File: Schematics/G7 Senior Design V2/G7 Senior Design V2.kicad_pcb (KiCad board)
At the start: 2 copper layers, 65 x 58.5 mm, 26 parts, among them IC1 TPS62122DRVR, IC3 CP2102N-A02-GQFN28, J1 87583-2010RLF, J2 PJ-051AH, Q1 SS8050-G, Q2 SS8050-G, U1 ESP32-WROOM-32-N4, U2 DWM1000

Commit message: Added Changes from Last Meeting
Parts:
- added C14-0.1uF1: CC0805KRX7R9BB104, SD V2 ESP32 Components:CC0805N_YAG, F.Cu at (167.4, 103.3)
- added C14-0.1uF3: CC0805KRX7R9BB104, SD V2 ESP32 Components:CC0805N_YAG, F.Cu at (188.8, 73.5)
- added C15-0.1uF4: CC0805KRX7R9BB104, SD V2 ESP32 Components:CC0805N_YAG, F.Cu at (167.4, 106.2)
- added C3-0.1uF4: CC0805KRX7R9BB104, SD V2 ESP32 Components:CC0805N_YAG, F.Cu at (167.4, 109.1)
- added C3-22uF2: LMK212BJ226MG-T, SD V2 ESP32 Components:CAP_LMK212AB7106MG-T_TAY, F.Cu at (168.1, 112.0)
- added C9-0.1uF2: CC0805KRX7R9BB104, SD V2 ESP32 Components:CC0805N_YAG, F.Cu at (188.8, 70.6)
- added LED1: HSMW-C170-U0000, SD V2 DW1000 Components:LEDC2012X90N, F.Cu at (184.2, 70.9)
- added LED2: HSMW-C170-U0000, SD V2 DW1000 Components:LEDC2012X90N, F.Cu at (184.2, 74.2)
- added LED3: HSMW-C170-U0000, SD V2 DW1000 Components:LEDC2012X90N, F.Cu at (184.2, 77.6)
- added LED4: HSMW-C170-U0000, SD V2 DW1000 Components:LEDC2012X90N, F.Cu at (184.2, 80.9)
- added LED5: HSMW-C170-U0000, SD V2 DW1000 Components:LEDC2012X90N, F.Cu at (190.4, 83.4)
- added R11-10K2: ERJ-6GEYJ103V, SD V2 USB to UART Components:RC0805N_PAN, F.Cu at (188.8, 76.4)
- added R3-0-Ohms1: RMCF0805ZT0R00, SD V2 USB to UART Components:STA_RMCF0805_STP, F.Cu at (189.1, 64.5)
- added R3-10K5: ERJ-6GEYJ103V, SD V2 USB to UART Components:RC0805N_PAN, F.Cu at (188.8, 79.2)
- added R3-10K6: ERJ-6GEYJ103V, SD V2 USB to UART Components:RC0805N_PAN, F.Cu at (190.1, 86.5)
- added R3-1K2: RG2012P-105-B-T5, SD V2 USB to UART Components:RES_1220_SUS, F.Cu at (193.1, 76.5)
- added R3-1K3: RG2012P-105-B-T5, SD V2 USB to UART Components:RES_1220_SUS, F.Cu at (186.6, 90.8)
- added R3-1K4: RG2012P-105-B-T5, SD V2 USB to UART Components:RES_1220_SUS, F.Cu at (186.6, 93.9)
- added R3-1K5: RG2012P-105-B-T5, SD V2 USB to UART Components:RES_1220_SUS, F.Cu at (190.4, 104.5)
- added S1: PTS_647_SN50_SMTR2_LFS, SD V2 ESP32 Components:SW_PTS_647_SN50_SMTR2_LFS, F.Cu at (161.1, 104.9)
- added S2: PTS_647_SN50_SMTR2_LFS, SD V2 ESP32 Components:SW_PTS_647_SN50_SMTR2_LFS, F.Cu at (161.1, 110.9)
- renumbered C3-0.1uF1 to C19-0.1uF1, C3-4.7uF1 to C20-4.7uF1, C3-22uF1 to C21-22uF1, C3-0.1uF2 to C22-0.1uF2, R3-10K3 to R21-10K3, R3-10K4 to R22-10K4, R3-10K1 to R23-10K1, R3-1K1 to R24-1K1, R3-22.1K1 to R25-22.1K1, R3-47.5K1 to R26-47.5K1
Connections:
- net Net-(U1-IO0) renamed /IO0
- C19-0.1uF1 pad 1: Net-(IC1-VOUT) -> Net-(IC3-VDD)
- C20-4.7uF1 pad 1: Net-(IC1-VOUT) -> Net-(IC3-VDD)
- C21-22uF1 pad 1: Net-(IC1-VOUT) -> Net-(IC3-VDD)
- C22-0.1uF2 pad 1: Net-(IC1-VOUT) -> Net-(IC3-VDD)
- IC3 pad 6: Net-(IC1-VOUT) -> Net-(IC3-VDD)
- IC3 pad 7: Net-(IC1-VOUT) -> Net-(IC3-VDD)
- Q1 pad 3: Net-(U1-EN) -> /EN
- R24-1K1 pad 1: Net-(IC1-VOUT) -> Net-(IC3-VDD)
- U1 pad 12: unconnected-(U1-IO27-Pad12) -> Net-(U1-IO27)
- U1 pad 2: Net-(IC1-VOUT) -> Net-(IC3-VDD)
- U1 pad 3: Net-(U1-EN) -> /EN
- U1 pad 6: unconnected-(U1-IO34-Pad6) -> Net-(U1-IO34)
- U1 pad 8: unconnected-(U1-IO32-Pad8) -> Net-(U1-IO32)
- U1 pad 9: unconnected-(U1-IO33-Pad9) -> Net-(U1-IO33)
- U2 pad 1: unconnected-(U2-EXTON-Pad1) -> Net-(U2-EXTON)
- U2 pad 12: unconnected-(U2-GPIO3/TXLED-Pad12) -> Net-(LED5-A)
- U2 pad 13: unconnected-(U2-GPIO2/RXLED-Pad13) -> Net-(LED1-A)
- U2 pad 14: unconnected-(U2-GPIO1/SFDLED-Pad14) -> Net-(LED2-A)
- U2 pad 15: unconnected-(U2-GPIO0/RXOKLED-Pad15) -> Net-(LED3-A)
- U2 pad 2: unconnected-(U2-WAKEUP-Pad2) -> Net-(U2-WAKEUP)
- U2 pad 22: unconnected-(U2-IRQ/GPIO8-Pad22) -> Net-(U1-IO34)
- U2 pad 3: unconnected-(U2-RSTN-Pad3) -> Net-(U2-RSTN)
- U2 pad 5: Net-(IC1-VOUT) -> Net-(IC3-VDD)
- U2 pad 6: Net-(IC1-VOUT) -> Net-(IC3-VDD)
- U2 pad 7: Net-(IC1-VOUT) -> Net-(IC3-VDD)
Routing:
- net Net-(U1-IO27): track 0.00 -> 32.7 mm, vias 0 -> 1
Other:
- board size 65 x 58.5 mm -> 85 x 58.5 mm

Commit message: Weeks Revision before Jungle of Words
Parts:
- moved R3-1K2 56.4 mm to (139.5, 94.0)
- moved LED4 48.0 mm to (139.3, 98.0), turned to -90 degrees
- moved LED3 46.3 mm to (142.7, 98.0), turned to -90 degrees
- moved LED2 45.0 mm to (146.0, 98.0), turned to -90 degrees
- moved LED1 44.2 mm to (149.3, 98.0), turned to -90 degrees
- moved LED5 40.1 mm to (153.0, 98.0), turned to -90 degrees
- moved R3-0-Ohms1 31.3 mm to (168.4, 88.0)
- moved S2 31.1 mm to (132.9, 97.9)
- moved S1 29.7 mm to (133.1, 114.9), turned to 180 degrees
- moved R11-10K2 28.6 mm to (164.1, 90.9)
- moved R3-10K5 28.6 mm to (164.1, 93.7)
- moved C14-0.1uF3 28.6 mm to (164.1, 88.0)
- moved C9-0.1uF2 28.6 mm to (164.1, 85.1)
- moved L1 26.2 mm to (190.4, 83.0)
- moved Cin-4.7uF1 25.8 mm to (195.9, 81.5)
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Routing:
- net GND: track 233.6 -> 405.5 mm, vias 2 -> 20
- net Net-(IC3-VDD): track 0.00 -> 148.4 mm, vias 0 -> 10
- net Net-(U1-IO19): track 37.4 -> 146.9 mm
- net /EN: track 0.00 -> 101.4 mm, vias 0 -> 5
- net Net-(U1-IO34): track 0.00 -> 71.9 mm, vias 0 -> 4
- net /IO0: track 40.6 -> 97.9 mm, vias 2 -> 4
- net Net-(U1-IO23): track 42.5 -> 98.2 mm
- net Net-(IC1-VOUT): track 144.9 -> 90.2 mm, vias 9 -> 8
- net Net-(U1-IO32): track 0.00 -> 46.3 mm, vias 0 -> 4
- net Net-(U1-IO33): track 0.00 -> 39.7 mm, vias 0 -> 4
- net Net-(U1-EN): track 40.0 -> 3.56 mm, vias 2 -> 0
- net Net-(U2-EXTON): track 0.00 -> 32.1 mm, vias 0 -> 2
- net Net-(U1-IO27): track 32.7 -> 62.2 mm, vias 1 -> 2
- net Net-(U2-WAKEUP): track 0.00 -> 28.8 mm, vias 0 -> 2
- net Net-(U1-IO4): track 23.4 -> 45.3 mm
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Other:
- board size 85 x 58.5 mm -> 85 x 73 mm

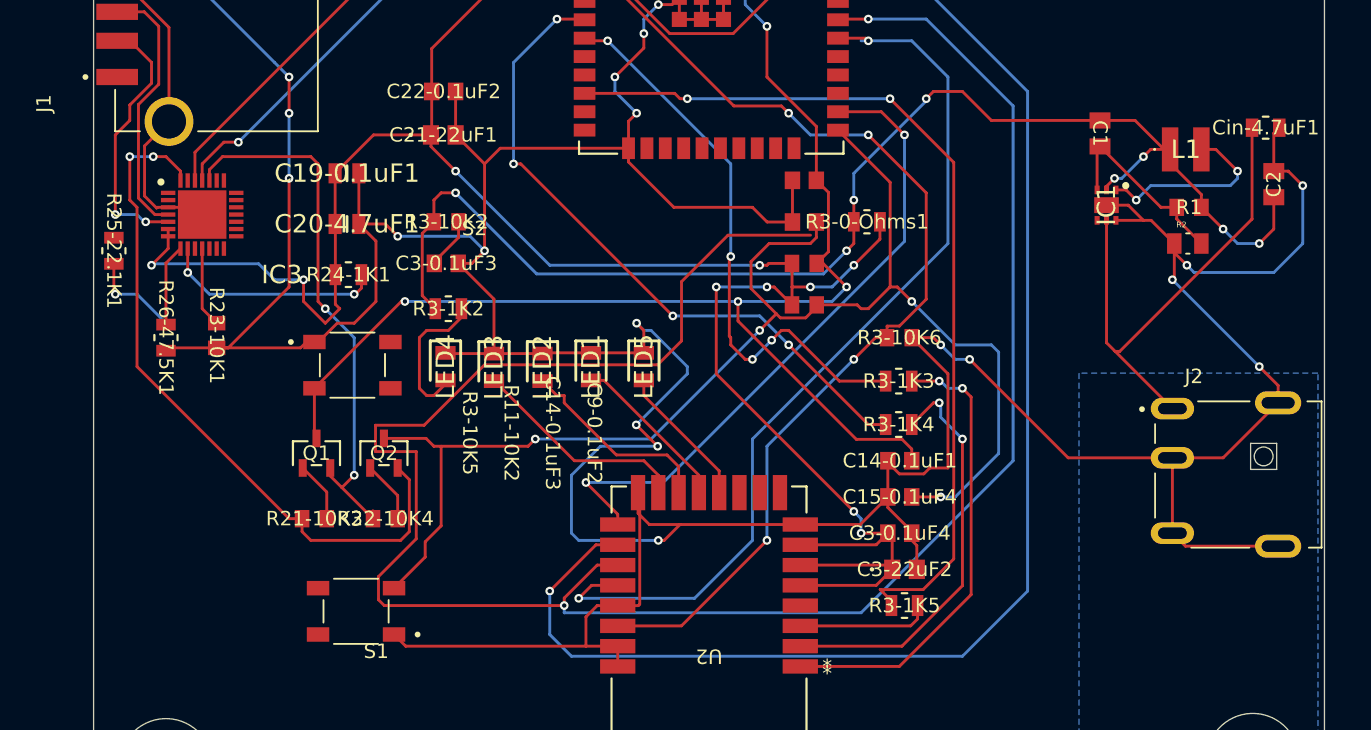
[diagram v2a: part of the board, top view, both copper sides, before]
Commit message: labels adjusted
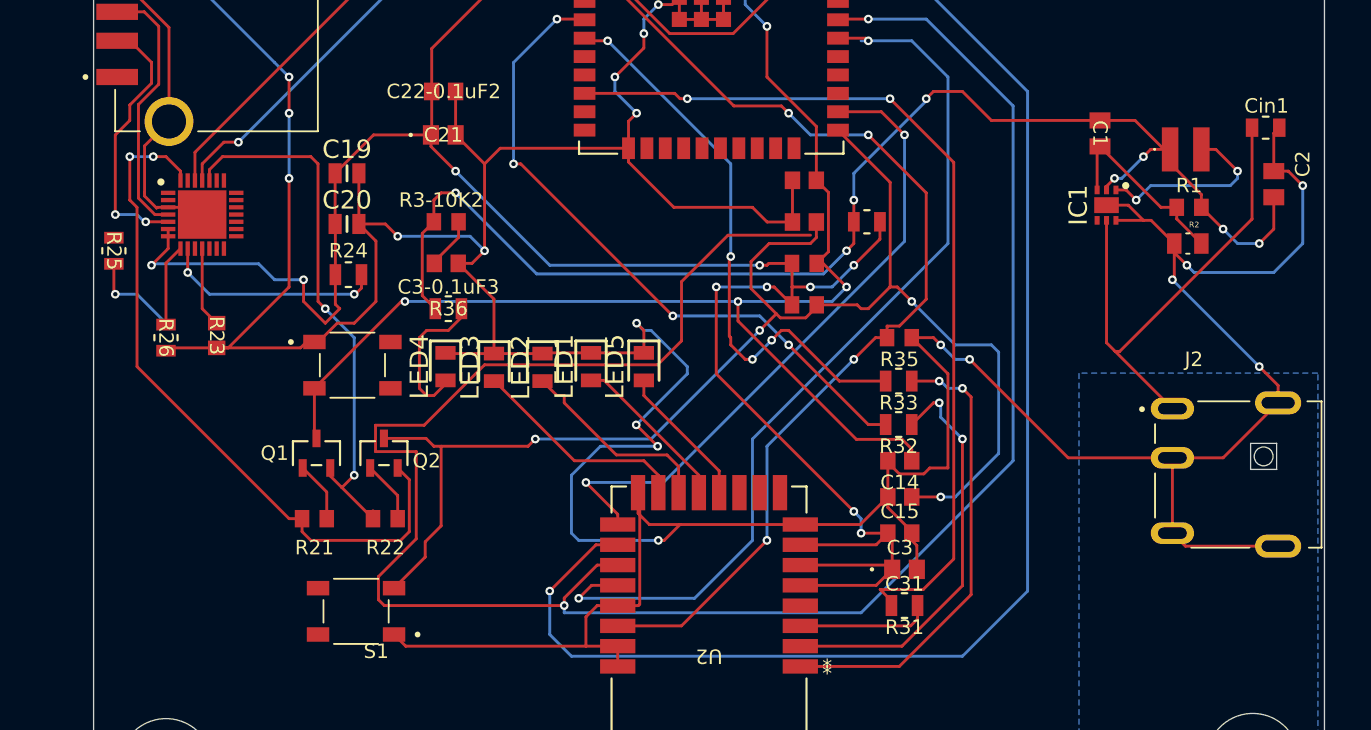
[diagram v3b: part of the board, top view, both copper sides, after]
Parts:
- C1: value CC0805JRNPO9BN220 -> C1
- C14: renamed from C14-0.1uF1; value CC0805KRX7R9BB104 -> C14
- C15: renamed from C15-0.1uF4; value CC0805KRX7R9BB104 -> C15
- C19: renamed from C19-0.1uF1; value GRM219C80J475KE19D -> C19
- C2: value 08056D475MAT2A -> C2
- C20: renamed from C20-4.7uF1; value GRM219C80J475KE19D -> C20
- C21: renamed from C21-22uF1; value LMK212BJ226MG-T -> C21
- C22-0.1uF2: value CC0805KRX7R9BB104 -> C22
- C3: renamed from C3-0.1uF4; value CC0805KRX7R9BB104 -> C6
- C31: renamed from C3-22uF2; value LMK212BJ226MG-T -> C5
- Cin1: renamed from Cin-4.7uF1; value VJ0805A4R7BXXPW1BC -> Cin
- IC1: value TPS62122DRVR -> REG
- IC3: value CP2102N-A02-GQFN28 -> UART
- J1: value 87583-2010RLF -> USB
- J2: value PJ-051AH -> JCK
- L1: value LPS3015-183MRC -> L1
- LED1: value HSMW-C170-U0000 -> LD2
- LED2: value HSMW-C170-U0000 -> LD3
- LED3: value HSMW-C170-U0000 -> LD4
- LED4: value HSMW-C170-U0000 -> LED1
- LED5: value HSMW-C170-U0000 -> LD5
- Q1: value SS8050-G -> T1
- Q2: value SS8050-G -> T2
- R1: value RC0805FR-07560KL -> R1
- R11: renamed from R11-10K2; value ERJ-6GEYJ103V -> R11
- R2: value CRGCQ0805F180K -> R2
- R21: renamed from R21-10K3; value ERJ-6GEYJ103V -> R21
- R22: renamed from R22-10K4; value ERJ-6GEYJ103V -> R22
- R23: renamed from R23-10K1; value ERJ-6GEYJ103V -> R23
- R24: renamed from R24-1K1; value RG2012P-105-B-T5 -> R24
- R25: renamed from R25-22.1K1; value RMCF0805FT22K1 -> R25
- R26: renamed from R26-47.5K1; value RMCF0805FT47K5 -> R26
- R3: renamed from R3-0-Ohms1; value RMCF0805ZT0R00 -> 0k
- R31: renamed from R3-1K5; value RG2012P-105-B-T5 -> RD1
- R32: renamed from R3-1K4; value RG2012P-105-B-T5 -> RD2
- R33: renamed from R3-1K3; value RG2012P-105-B-T5 -> RD3
- R34: renamed from R3-10K5; value ERJ-6GEYJ103V -> R3
- R35: renamed from R3-10K6; value ERJ-6GEYJ103V -> R31
- R36: renamed from R3-1K2; value RG2012P-105-B-T5 -> R3
- S1: value PTS_647_SN50_SMTR2_LFS -> S1
- S2: value PTS_647_SN50_SMTR2_LFS -> S3

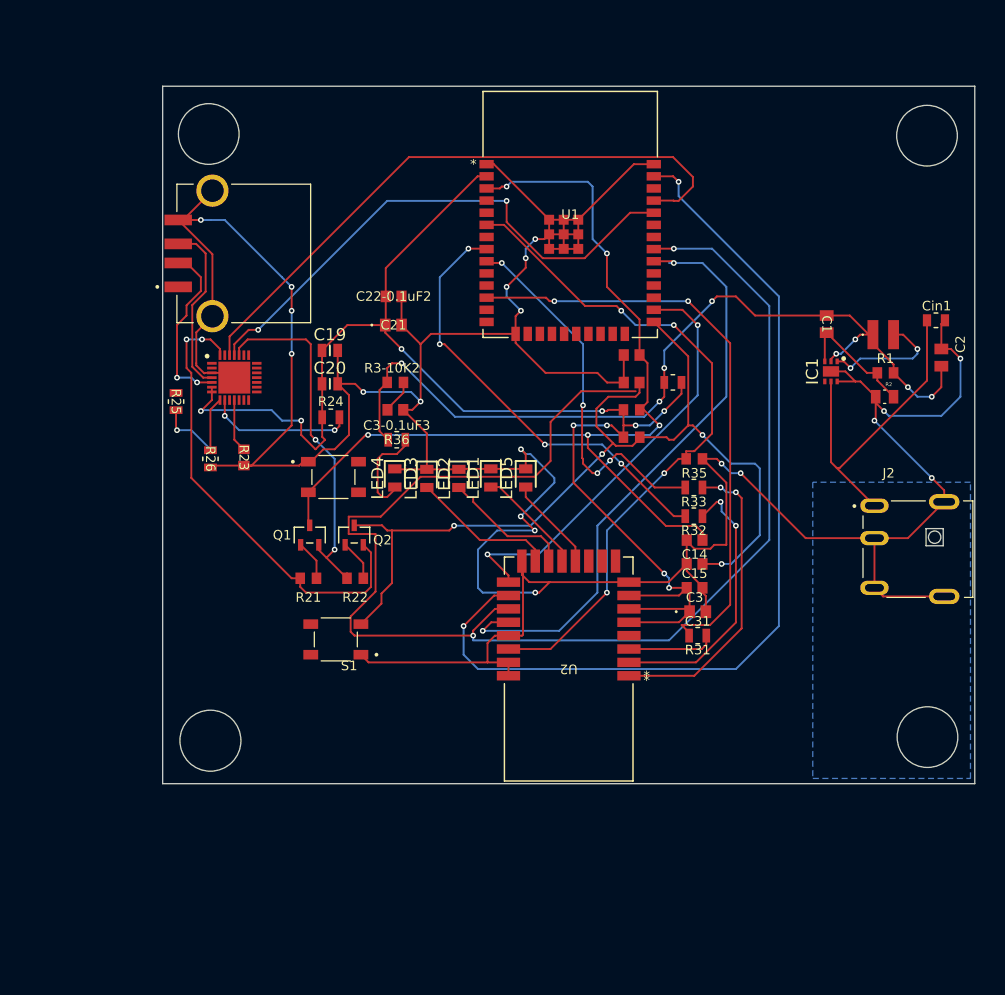
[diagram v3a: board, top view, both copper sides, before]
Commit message: First Version to be Ordered from JLCPCB
Associated schematic with first Gerber file to be sent out to JLCPCB to be fabricated.
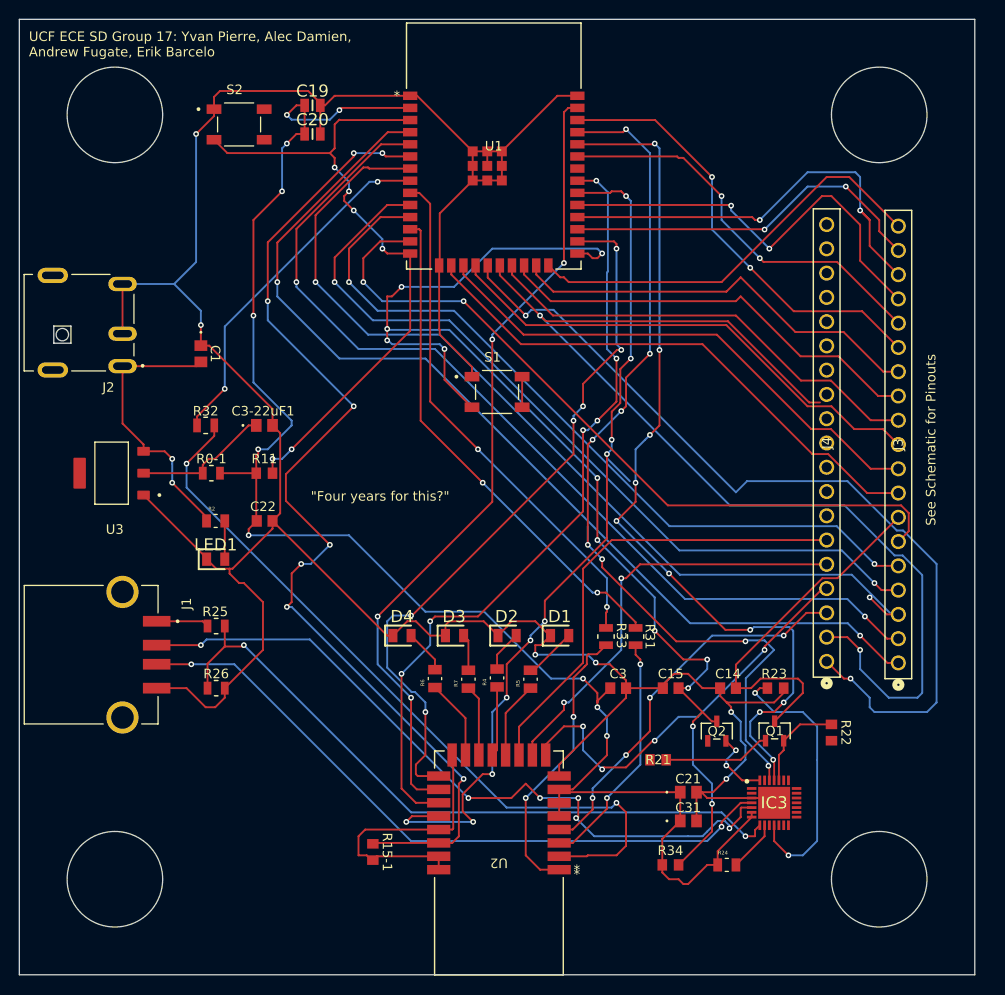
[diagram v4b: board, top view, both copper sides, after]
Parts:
- removed C14-0.1uF3, C3-0.1uF3, C9-0.1uF2: CC0805KRX7R9BB104, SD V2 ESP32 Components:CC0805N_YAG
- removed C2: C2, SD V2 Voltage Regulator Components:Cout-4.7uF CAP_0805N_AVX
- removed C22-0.1uF2: C22, SD V2 ESP32 Components:CC0805N_YAG
- removed Cin1: Cin, SD V2 Voltage Regulator Components:Cin-CAP_VJ0805_VIS
- removed IC1: REG, SD V2 Voltage Regulator Components:SON65P200X200X80-7N
- removed L1: L1, SD V2 Voltage Regulator Components:L1-18uH LPS3015183MRC
- removed LED2: LD3, SD V2 DW1000 Components:LEDC2012X90N
- removed LED3: LD4, SD V2 DW1000 Components:LEDC2012X90N
- removed LED4: LED1, SD V2 DW1000 Components:LEDC2012X90N
- removed LED5: LD5, SD V2 DW1000 Components:LEDC2012X90N
- removed R1: R1, SD V2 Voltage Regulator Components:R1-560K RC0805N_YAG
- removed R3: 0k, SD V2 USB to UART Components:STA_RMCF0805_STP
- removed R3-10K2: ERJ-6GEYJ103V, SD V2 USB to UART Components:RC0805N_PAN
- removed R35: R31, SD V2 USB to UART Components:RC0805N_PAN
- removed R36: R3, SD V2 USB to UART Components:RES_1220_SUS
- added C22: 0.1uF, SD V2 ESP32 Components:CC0805N_YAG, F.Cu at (125.7, 102.5)
- added C3-22uF1: LMK212BJ226MG-T, SD V2 ESP32 Components:CAP_LMK212AB7106MG-T_TAY, F.Cu at (125.6, 92.5)
- added D1: LD1, SD V2 DW1000 Components:LEDC2012X90N, F.Cu at (156.6, 114.5)
- added D2: LD2, SD V2 DW1000 Components:LEDC2012X90N, F.Cu at (151.1, 114.5)
- added D3: LD3, SD V2 DW1000 Components:LEDC2012X90N, F.Cu at (145.6, 114.5)
- added D4: LD4, SD V2 DW1000 Components:LEDC2012X90N, F.Cu at (140.1, 114.5)
- added J3: PPTC191LFBN-RC, SD V2 ESP32 Components:CONN19_PPTC191LFBN-RC_SUL, F.Cu at (192.0, 117.4)
- added J4: PPTC191LFBN-RC, SD V2 ESP32 Components:CONN19_PPTC191LFBN-RC_SUL, F.Cu at (184.5, 117.2)
- added R0-1: 0K, SD V2 Voltage Regulator Components:STA_RMCF0805_STP, F.Cu at (120.1, 97.5)
- added R15-1: 10K, SD V2 USB to UART Components:RC0805N_PAN, F.Cu at (137.0, 137.1)
- added R4: CRGCQ0805J470R, SD V2 DW1000 Components:RESC2012X65N, F.Cu at (150.0, 118.9)
- added R5: CRGCQ0805J470R, SD V2 DW1000 Components:RESC2012X65N, F.Cu at (153.5, 119.1)
- added R6: CRGCQ0805J470R, SD V2 DW1000 Components:RESC2012X65N, F.Cu at (143.5, 119.0)
- added R7: CRGCQ0805J470R, SD V2 DW1000 Components:RESC2012X65N, F.Cu at (147.0, 119.1)
- added U3: AMS1117-3.3, SD V2 Voltage Regulator Components:SOT229P700X180-4N, F.Cu at (109.7, 97.5)
- C1: value C1 -> 22uF; footprint SD V2 Voltage Regulator Components:Cff-22pF CAP_CC0805_YAG -> SD V2 ESP32 Components:CAP_LMK212AB7106MG-T_TAY
- C14: value C14 -> 0.1uF
- C19: value C19 -> 0.1uF
- C20: value C20 -> 4.7uF
- C21: value C21 -> 22uF
- LED1: value LD2 -> RED
- R2: value R2 -> 2K; footprint SD V2 Voltage Regulator Components:R2-180K RESC2012X65N -> SD V2 USB to UART Components:RESC2012X60N
- R21: value R21 -> 10K
- R22: value R22 -> 10K
- R23: value R23 -> 10K
- R24: value R24 -> 2K; footprint SD V2 USB to UART Components:RES_1220_SUS -> SD V2 USB to UART Components:RESC2012X60N
- R25: value R25 -> 22.1K
- R26: value R26 -> 47.5K
- R34: value R3 -> 10K
- S2: value S3 -> S2
- moved J2 90.9 mm to (106.2, 81.8), turned to 180 degrees
- moved IC3 71.9 mm to (179.0, 132.0)
- moved R2 71.2 mm to (120.5, 102.5)
- moved C1 65.6 mm to (119.0, 85.0)
- moved R24 62.6 mm to (174.0, 138.5)
- moved R23 60.7 mm to (179.1, 120.0), turned to 0 degrees
- moved C21 57.8 mm to (170.0, 130.9)
- moved Q1 52.8 mm to (179.0, 124.5)
- moved R22 52.4 mm to (185.0, 124.6), turned to -90 degrees
- moved R32 52.0 mm to (119.5, 92.5)
- moved R34 44.9 mm to (168.1, 138.5)
- moved Q2 43.1 mm to (173.0, 124.5)
- moved J1 43.0 mm to (110.8, 116.5), turned to -90 degrees
- moved R21 41.2 mm to (166.9, 127.5)
- moved R11 39.0 mm to (125.6, 97.5)
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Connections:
- C1 pad 1: Net-(IC1-VOUT) -> GND
- C1 pad 2: Net-(IC1-FB) -> Net-(U3-VIN)
- J1 pad S1: GND -> unconnected-(J1-SHIELD-PadS1)
- J1 pad S2: GND -> unconnected-(J1-SHIELD__1-PadS2)
- J2 pad 1: Net-(IC1-EN) -> Net-(U3-VIN)
- J2 pad S1: GND -> unconnected-(J2-SHIELD-PadS1)
- J2 pad S2: GND -> unconnected-(J2-SHIELD__1-PadS2)
- R2 pad 1: GND -> Net-(U3-VIN)
- R2 pad 2: Net-(IC1-FB) -> Net-(LED1-A)
- U1 pad 10: unconnected-(U1-IO25-Pad10) -> Net-(U1-IO25)
- U1 pad 11: unconnected-(U1-IO26-Pad11) -> Net-(U1-IO26)
- U1 pad 13: unconnected-(U1-IO14-Pad13) -> Net-(U1-IO14)
- U1 pad 14: unconnected-(U1-IO12-Pad14) -> /EN
- U1 pad 16: unconnected-(U1-IO13-Pad16) -> Net-(U1-IO13)
- U1 pad 17: unconnected-(U1-SD2-Pad17) -> Net-(U1-SD2)
- U1 pad 18: unconnected-(U1-SD3-Pad18) -> Net-(U1-SD3)
- U1 pad 19: unconnected-(U1-CMD-Pad19) -> Net-(U1-CMD)
- U1 pad 20: unconnected-(U1-CLK-Pad20) -> Net-(U1-CLK)
- U1 pad 21: unconnected-(U1-SD0-Pad21) -> Net-(U1-SD0)
- U1 pad 22: unconnected-(U1-SD1-Pad22) -> Net-(U1-SD1)
- U1 pad 23: unconnected-(U1-IO15-Pad23) -> Net-(U1-IO15)
- U1 pad 24: unconnected-(U1-IO2-Pad24) -> Net-(U1-IO2)
- U1 pad 27: unconnected-(U1-IO16-Pad27) -> Net-(U1-IO16)
- U1 pad 28: unconnected-(U1-IO17-Pad28) -> Net-(U1-IO17)
- U1 pad 29: unconnected-(U1-IO5-Pad29) -> Net-(U1-IO5)
- U1 pad 33: unconnected-(U1-IO21-Pad33) -> Net-(U1-IO21)
- U1 pad 36: unconnected-(U1-IO22-Pad36) -> Net-(U1-IO22)
- U1 pad 4: unconnected-(U1-SENSOR_VP-Pad4) -> Net-(U1-SENSOR_VP)
- U1 pad 5: unconnected-(U1-SENSOR_VN-Pad5) -> Net-(U1-SENSOR_VN)
- U1 pad 7: unconnected-(U1-IO35-Pad7) -> Net-(U1-IO35)
- U2 pad 10: unconnected-(U2-GPIO5/EXTTXE/SPIPOL-Pad10) -> Net-(U2-GPIO5/EXTTXE/SPIPOL)
- U2 pad 11: unconnected-(U2-GPIO4/EXTPA-Pad11) -> Net-(U2-GPIO4/EXTPA)
- U2 pad 13: Net-(LED1-A) -> Net-(U2-GPIO2/RXLED)
- U2 pad 4: unconnected-(U2-GPIO7-Pad4) -> Net-(U2-GPIO7)
- U2 pad 9: unconnected-(U2-GPIO6/EXTRXE/SPIPHA-Pad9) -> Net-(U2-GPIO6/EXTRXE/SPIPHA)
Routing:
- net Net-(U1-CLK): track 0.00 -> 117.6 mm, vias 0 -> 2
- net Net-(U1-SENSOR_VP): track 0.00 -> 105.2 mm, vias 0 -> 2
- net Net-(U1-SENSOR_VN): track 0.00 -> 99.9 mm, vias 0 -> 2
- net Net-(U1-IO35): track 0.00 -> 98.2 mm, vias 0 -> 2
- net Net-(U1-CMD): track 0.00 -> 91.3 mm, vias 0 -> 2
- net Net-(IC1-VOUT): track 90.2 -> 0.00 mm, vias 8 -> 0
- net Net-(U1-IO25): track 0.00 -> 85.1 mm, vias 0 -> 2
- net Net-(U1-IO26): track 0.00 -> 81.1 mm, vias 0 -> 2
- net Net-(U1-IO14): track 0.00 -> 78.7 mm, vias 0 -> 2
- net GND: track 405.5 -> 329.3 mm, vias 20 -> 6
- net Net-(U1-IO19): track 146.9 -> 83.5 mm, vias 2 -> 6
- net Net-(IC3-VBUS): track 12.1 -> 72.4 mm, vias 1 -> 2
- net Net-(IC3-D-): track 18.4 -> 76.5 mm, vias 2 -> 6
- net Net-(U1-IO13): track 0.00 -> 57.2 mm
- net Net-(U1-SD2): track 0.00 -> 54.9 mm
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- removed copper zone on B.Cu, net GND
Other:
- board size 85 x 73 mm -> 100 x 100 mm
- board text added: "See Schematic for Pinouts"
- board text added: "UCF ECE SD Group 17: Yvan Pierre, Alec Damien, Andrew Fugate, Erik Barcelo"
- board text added: "{dblquote}Four years for this?{dblquote}"
